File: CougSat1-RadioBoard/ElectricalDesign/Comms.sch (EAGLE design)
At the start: 409 parts, among them J1 700mm Antenna, J2 CougSat Card, J3 230mm Antenna, J4 SWD, Q1 DMN53D0LDW, Q2 DMN53D0LDW, Q3 DMN53D0LDW, Q4 CSD25402Q3A, Q5 CSD25402Q3A, U1 AD8515, U10 AD8515, U11 AD8515, U12 TXS0102DQM, U13 ADF4360, U14 MAAM-011229, U15 INA199C2, U16 AD8515, U17 AD8515, U18 LP5907MFX-3.1, U19 HMC545A, U2 AD8515, U20 INA199C1, U21 TPS61236, U22 AD8345, U23 AD9761, U24 TXS0102DQM, U25 TXS0102DQM, U26 TXS0102DQM, U27 MMZ09332B, U28 AD8515, U29 ADF4360, U3 AD7291, U30 TXS0102DQM, U31 INA199C2, U32 TXS0102DQM, U33 LP5907MFX-3.1, U34 MAAM-011229, U35 TXS0102DQM, U36 TXS0102DQM, U37 AD9761, U38 AD8346, U39 TXS0102DQM, U4 AD7291, U40 STM32L496VGT, U41 HMC452QS16G, U42 TXS0102DQM, U43 INA199C2, U44 ADF4360, U45 LP5907MFX-3.1, U46 IS25LP016D, U47 IS25LP016D, U48 GRF2133, U49 INA199C1, U5 MAAM-011229, U6 AD8348, U7 AD7291, U8 MAAM-011229, U9 TXS0102DQM, Y1 19.68MHz ±2.5ppm, Y2 19.68MHz ±2.5ppm, Y3 8MHz ±10ppm, Y4 32.768kHz ±10ppm, Y5 19.68MHz ±2.5ppm

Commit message: Updated off-sheet labels and exported gerbers
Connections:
- net PC_3.1V-1: now also U40C.PC13
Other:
- note added: "10A3>"
- note added: "10A5>"
- note added: "10B1>"
- note added: "10C2>"
- note added: "10C6>"
- note added: "10D3>"
- note added: "11A3>"
- note added: "11A5>"
- note added: "11B1>"
- note added: "11B3> 11C3>"
- note added: "11C1>"
- note added: "11D1>"
- note added: "12A1>"
- note added: "12A2>"
- note added: "12B2>"
- note added: "12C3>"
- note added: "13A1>"
- note added: "13A2>"
- note added: "13B2>"
- note added: "13C1>"
- note added: "13C3>"
- note added: "13D2>"
- note added: "13D5>"
- note added: "14B1> 14B3> 14C2>"
- note added: "14C5>"
- note added: "14D3>"
- note added: "15A1>"
- note added: "15A4>"
- note added: "15B1>"
- note added: "15B2>"
- note added: "15B3>"
- note added: "15B4>"
- note added: "230mm Downlink"
- note added: "4A1> 5D4>"
- note added: "4A4>"
- note added: "4A4> 9A1> 10A1> 11A1>"
- note added: "4B1>"
- note added: "4B2>"
- note added: "4B3>"
- note added: "4B4>"
- note added: "4B6>"
- note added: "4C1>"
- note added: "4C4>"
- note added: "4D2>"
- note added: "5B4>"
- note added: "6A3> 6A6> 6C6>"
- note added: "6C1>"
- note added: "700mm Downlink"
- note added: "700mm Uplink"
- note added: "7A3>"
- note added: "7B2>"
- note added: "7B6>"
- note added: "7C3>"
- note added: "8A2>"
- note added: "8A3>"
- note added: "8A5>"
- note added: "8B2>"
- note added: "8B3>"
- note added: "8B5>"
- note added: "8C2>"
- note added: "8C3>"
- note added: "8C5>"
- note added: "8D2>"
- note added: "9A3>"
- note added: "9A5>"
- note added: "9B1>"
- note added: "9B2> 10B2>"
- note added: "9C2>"
- note added: "9C6>"
- note added: "9D3>"
- note added: "<10B3"
- note added: "<11B3"
- note added: "<11C3"
- note added: "<11C5"
- note added: "<11D3"
- note added: "<14B1"
- note added: "<4A1 <5C4"
- note added: "<4A1> <5D4"
- note added: "<4A4"
- note added: "<4C2"
- note added: "<4C2>"
- note added: "<4C6"
- note added: "<4D2"
- note added: "<5A4"
- note added: "<5B4"
- note added: "<5C4"
- note added: "<6A1"
- note added: "<6A4"
- note added: "<6B1"
- note added: "<9B3"
- note added: "Page 10: Baseband & Carrier - 700 Page 11: Baseband & Carrier - 700 Page 12: 230mm Downlink Page 13: 700mm Downlink Page 14: 700mm Uplink Amplifiers Page 15: Demodulator Page 16: Mechanical"
- note added: "Page 11"
- note added: "Page 1: Block Diagram Page 2: RF Diagram Page 3: Power Rails Page 4: µController Page 5: Buffers Page 6: ADCs Page 7: Regulator Page 8: Power Switching & LDOs Page 9: Baseband & Carrier - 230"
- note added: "Pages 10"
- note added: "Pages 10/11"
- note added: "Pages 12"
- note added: "Pages 13"
- note added: "Pages 14"
- note added: "Pages 15"
- note added: "Pages 4"
- note added: "Pages 5"
- note added: "Pages 6"
- note added: "Pages 7"
- note added: "Pages 9"
- note added: "SWD Header"
- note removed: "14B1>"
- note removed: "6xx>"
- note removed: "7xx>"
- note removed: "<4B3"
- note removed: "<4xx"
- note removed: "Page 10: Differential Drivers Page 11: 230mm Downlink Page 12: 700mm Downlink Page 13: 700mm Downlink Amplifers Page 14: Demodulator Page 15: Flash Memory Page 16: Mechanical"
- note removed: "Page 1: Block Diagram Page 2: RF Diagram Page 3: Power Rails Page 4: µController Page 5: ADCs Page 6: Regulators Page 7: Power Switching & LDOs Page 8: RF Clocks - 700mm Page 9: RF Clock - 230mm"
- note removed: "Page X"
- note removed: "Pages X"
- moved on the sheet: C183, C184, R94, R95, U46, U47

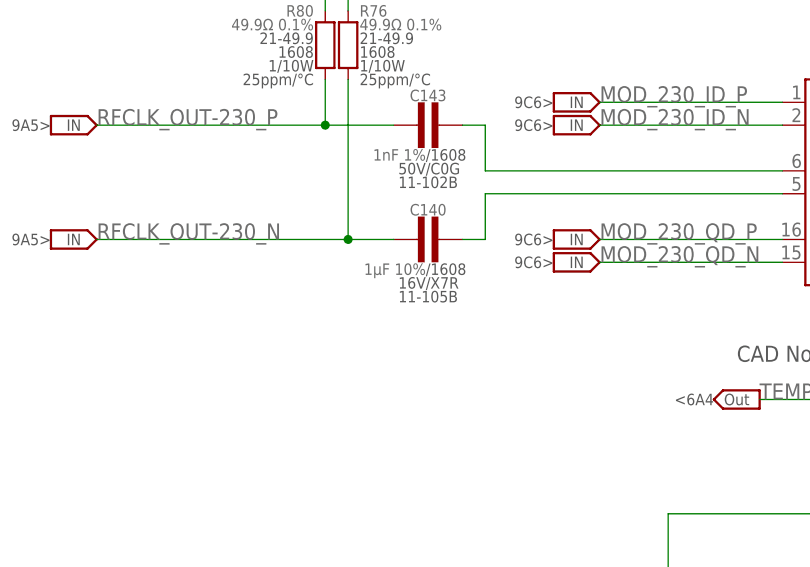
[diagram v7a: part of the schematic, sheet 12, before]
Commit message: Created mCAD, fixed silkscreen
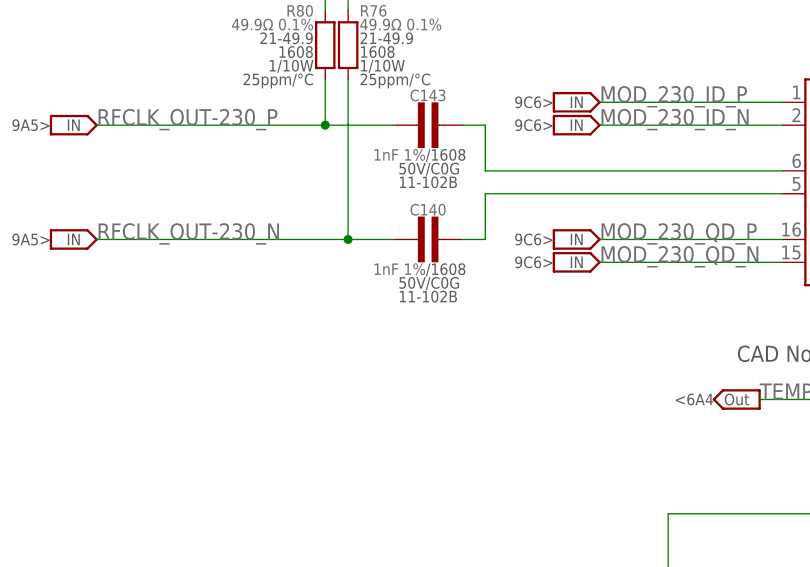
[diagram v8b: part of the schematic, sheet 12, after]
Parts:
- C140: value 1µF 10% -> 1nF 1%; device CougsInSpace-Capacitors:CAP-H-1UF-B-1608 -> CougsInSpace-Capacitors:CAP-H-1NF-B-1608
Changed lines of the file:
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@@
 <setting verticaltext="up"/>
 </settings>
-<grid distance="1" unitdist="mm" unit="mm" style="lines" multiple="1" display="yes" altdistance="0.1" altunitdist="mm" altunit="mm"/>
+<grid distance="0.1" unitdist="inch" unit="inch" style="lines" multiple="1" display="no" altdistance="0.01" altunitdist="inch" altunit="inch"/>
 <layers>
-<layer number="1" name="Top" color="4" fill="1" visible="no" active="no"/>
-<layer number="2" name="Route2" color="16" fill="10" visible="no" active="no"/>
-<layer number="3" name="Route3" color="17" fill="1" visible="no" active="no"/>
-<layer number="4" name="Route4" color="18" fill="1" visible="no" active="no"/>
-<layer number="5" name="Route5" color="19" fill="1" visible="no" active="no"/>
-<layer number="6" name="Route6" color="25" fill="1" visible="no" active="no"/>
-<layer number="7" name="Route7" color="26" fill="1" visible="no" active="no"/>
-<layer number="8" name="Route8" color="27" fill="1" visible="no" active="no"/>
-<layer number="9" name="Route9" color="28" fill="1" visible="no" active="no"/>
-<layer number="10" name="Route10" color="29" fill="1" visible="no" active="no"/>
-<layer number="11" name="Route11" color="30" fill="1" visible="no" active="no"/>
-<layer number="12" name="Route12" color="20" fill="1" visible="no" active="no"/>
-<layer number="13" name="Route13" color="21" fill="1" visible="no" active="no"/>
-<layer number="14" name="Route14" color="22" fill="1" visible="no" active="no"/>
-<layer number="15" name="Route15" color="23" fill="11" visible="no" active="no"/>
-<layer number="16" name="Bottom" color="1" fill="1" visible="no" active="no"/>
-<layer number="17" name="Pads" color="2" fill="1" visible="no" active="no"/>
-<layer number="18" name="Vias" color="2" fill="1" visible="no" active="no"/>
-<layer number="19" name="Unrouted" color="6" fill="1" visible="no" active="no"/>
-<layer number="20" name="Dimension" color="24" fill="1" visible="no" active="no"/>
-<layer number="21" name="tPlace" color="7" fill="1" visible="no" active="no"/>
-<layer number="22" name="bPlace" color="7" fill="1" visible="no" active="no"/>
-<layer number="23" name="tOrigins" color="15" fill="1" visible="no" active="no"/>
-<layer number="24" name="bOrigins" color="15" fill="1" visible="no" active="no"/>
-<layer number="25" name="tNames" color="7" fill="1" visible="no" active="no"/>
-<layer number="26" name="bNames" color="7" fill="1" visible="no" active="no"/>
-<layer number="27" name="tValues" color="7" fill="1" visible="no" active="no"/>
-<layer number="28" name="bValues" color="7" fill="1" visible="no" active="no"/>
+<layer number="1" name="Top" color="4" fill="1" visible="yes" active="no"/>
+<layer number="2" name="Route2" color="16" fill="1" visible="yes" active="no"/>
+<layer number="3" name="Route3" color="17" fill="1" visible="yes" active="no"/>
+<layer number="4" name="Route4" color="18" fill="1" visible="yes" active="no"/>
+<layer number="5" name="Route5" color="19" fill="1" visible="yes" active="no"/>
+<layer number="6" name="Route6" color="25" fill="1" visible="yes" active="no"/>
+<layer number="7" name="Route7" color="26" fill="1" visible="yes" active="no"/>
+<layer number="8" name="Route8" color="27" fill="1" visible="yes" active="no"/>
+<layer number="9" name="Route9" color="28" fill="1" visible="yes" active="no"/>
+<layer number="10" name="Route10" color="29" fill="1" visible="yes" active="no"/>
+<layer number="11" name="Route11" color="30" fill="1" visible="yes" active="no"/>
+<layer number="12" name="Route12" color="20" fill="1" visible="yes" active="no"/>
+<layer number="13" name="Route13" color="21" fill="1" visible="yes" active="no"/>
+<layer number="14" name="Route14" color="22" fill="1" visible="yes" active="no"/>
+<layer number="15" name="Route15" color="23" fill="1" visible="yes" active="no"/>
+<layer number="16" name="Bottom" color="1" fill="1" visible="yes" active="no"/>
+<layer number="17" name="Pads" color="2" fill="1" visible="yes" active="no"/>
+<layer number="18" name="Vias" color="2" fill="1" visible="yes" active="no"/>
+<layer number="19" name="Unrouted" color="6" fill="1" visible="yes" active="no"/>
+<layer number="20" name="Dimension" color="24" fill="1" visible="yes" active="no"/>
+<layer number="21" name="tPlace" color="7" fill="1" visible="yes" active="no"/>
+<layer number="22" name="bPlace" color="7" fill="1" visible="yes" active="no"/>
+<layer number="23" name="tOrigins" color="15" fill="1" visible="yes" active="no"/>
+<layer number="24" name="bOrigins" color="15" fill="1" visible="yes" active="no"/>
+<layer number="25" name="tNames" color="7" fill="1" visible="yes" active="no"/>
+<layer number="26" name="bNames" color="7" fill="1" visible="yes" active="no"/>
+<layer number="27" name="tValues" color="7" fill="1" visible="yes" active="no"/>
+<layer number="28" name="bValues" color="7" fill="1" visible="yes" active="no"/>
 <layer number="29" name="tStop" color="7" fill="3" visible="no" active="no"/>
 <layer number="30" name="bStop" color="7" fill="6" visible="no" active="no"/>
@@
 <layer number="35" name="tGlue" color="7" fill="4" visible="no" active="no"/>
 <layer number="36" name="bGlue" color="7" fill="5" visible="no" active="no"/>
-<layer number="37" name="tTest" color="7" fill="1" visible="no" active="no"/>
-<layer number="38" name="bTest" color="7" fill="1" visible="no" active="no"/>
+<layer number="37" name="tTest" color="7" fill="1" visible="yes" active="no"/>
+<layer number="38" name="bTest" color="7" fill="1" visible="yes" active="no"/>
 <layer number="39" name="tKeepout" color="4" fill="11" visible="no" active="no"/>
 <layer number="40" name="bKeepout" color="1" fill="11" visible="no" active="no"/>
@@
 <layer number="44" name="Drills" color="7" fill="1" visible="no" active="no"/>
 <layer number="45" name="Holes" color="7" fill="1" visible="no" active="no"/>
-<layer number="46" name="Milling" color="3" fill="1" visible="no" active="no"/>
-<layer number="47" name="Measures" color="7" fill="1" visible="no" active="no"/>
-<layer number="48" name="Document" color="7" fill="1" visible="no" active="no"/>
-<layer number="49" name="Reference" color="7" fill="1" visible="no" active="no"/>
-<layer number="50" name="dxf" color="7" fill="1" visible="no" active="no"/>
-<layer number="51" name="tDocu" color="7" fill="1" visible="no" active="no"/>
-<layer number="52" name="bDocu" color="7" fill="1" visible="no" active="no"/>
-<layer number="53" name="tGND_GNDA" color="7" fill="9" visible="no" active="no"/>
-<layer number="54" name="bGND_GNDA" color="1" fill="9" visible="no" active="no"/>
-<layer number="56" name="wert" color="7" fill="1" visible="no" active="no"/>
-<layer number="57" name="tCAD" color="7" fill="1" visible="no" active="no"/>
-<layer number="58" name="bCAD" color="9" fill="1" visible="no" active="no"/>
-<layer number="59" name="tCarbon" color="7" fill="1" visible="no" active="no"/>
-<layer number="60" name="bCarbon" color="7" fill="1" visible="no" active="no"/>
+<layer number="46" name="Milling" color="3" fill="1" visible="yes" active="no"/>
+<layer number="47" name="Measures" color="7" fill="1" visible="yes" active="no"/>
+<layer number="48" name="Document" color="7" fill="1" visible="yes" active="no"/>
+<layer number="49" name="Reference" color="7" fill="1" visible="yes" active="no"/>
+<layer number="50" name="dxf" color="7" fill="1" visible="yes" active="no"/>
+<layer number="51" name="tDocu" color="7" fill="1" visible="yes" active="no"/>
+<layer number="52" name="bDocu" color="7" fill="1" visible="yes" active="no"/>
+<layer number="53" name="tGND_GNDA" color="7" fill="9" visible="yes" active="no"/>
+<layer number="54" name="bGND_GNDA" color="1" fill="9" visible="yes" active="no"/>
+<layer number="56" name="wert" color="7" fill="1" visible="yes" active="no"/>
+<layer number="57" name="tCAD" color="7" fill="1" visible="yes" active="no"/>
+<layer number="58" name="bCAD" color="9" fill="1" visible="yes" active="no"/>
+<layer number="59" name="tCarbon" color="7" fill="1" visible="yes" active="no"/>
+<layer number="60" name="bCarbon" color="7" fill="1" visible="yes" active="no"/>
 <layer number="88" name="SimResults" color="9" fill="1" visible="yes" active="yes"/>
 <layer number="89" name="SimProbes" color="9" fill="1" visible="yes" active="yes"/>
@@
 <part name="R29" library="CougsInSpace-Resistors" deviceset="RES-V" device="-1608" technology="-470R" value="470Ω 0.5%"/>
 <part name="U38" library="CougsInSpace-RF" deviceset="AD834X" device="" technology="6" value="AD8346"/>
-<part name="C140" library="CougsInSpace-Capacitors" deviceset="CAP-H" device="-1608" technology="-1UF-B" value="1µF 10%"/>
+<part name="C140" library="CougsInSpace-Capacitors" deviceset="CAP-H" device="-1608" technology="-1NF-B" value="1nF 1%"/>
 <part name="C143" library="CougsInSpace-Capacitors" deviceset="CAP-H" device="-1608" technology="-1NF-B" value="1nF 1%"/>
 <part name="R76" library="CougsInSpace-Resistors" deviceset="RES-V" device="-1608" technology="-49.9" value="49.9Ω 0.1%"/>
